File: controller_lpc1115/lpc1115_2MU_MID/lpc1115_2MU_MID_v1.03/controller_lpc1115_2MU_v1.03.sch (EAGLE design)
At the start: 57 parts, among them IC1 LPC1115, IC2 BD9G101, Q1 BC856, Q2 BC847C, Q3 BCP52, Q4 ASFL

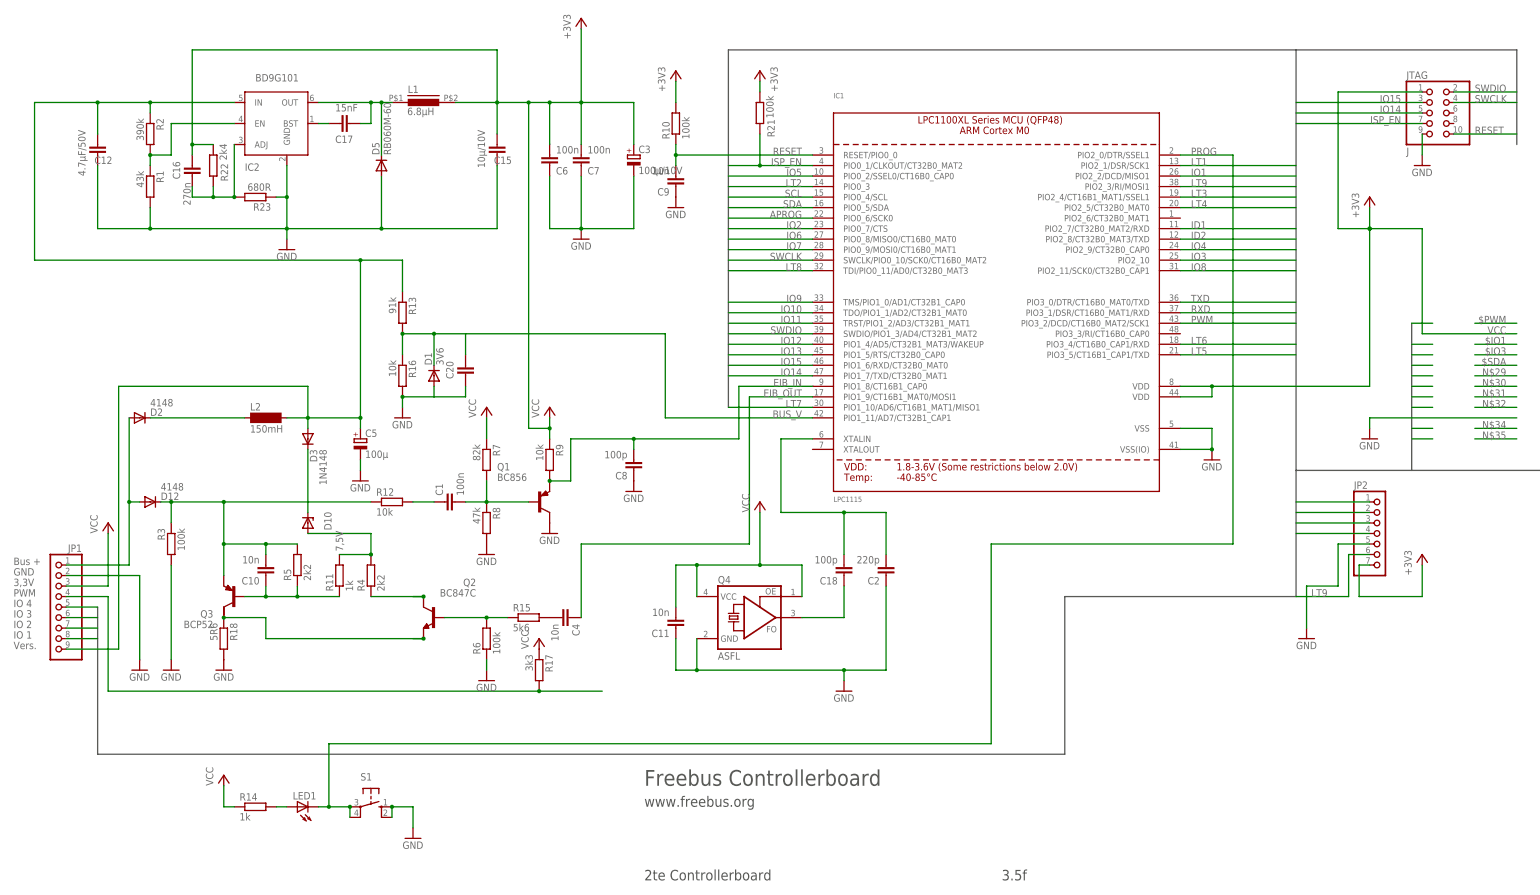
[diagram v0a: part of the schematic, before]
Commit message: Fix/add JP1 and JP2 pininfo for 2MU lpc1115 controller
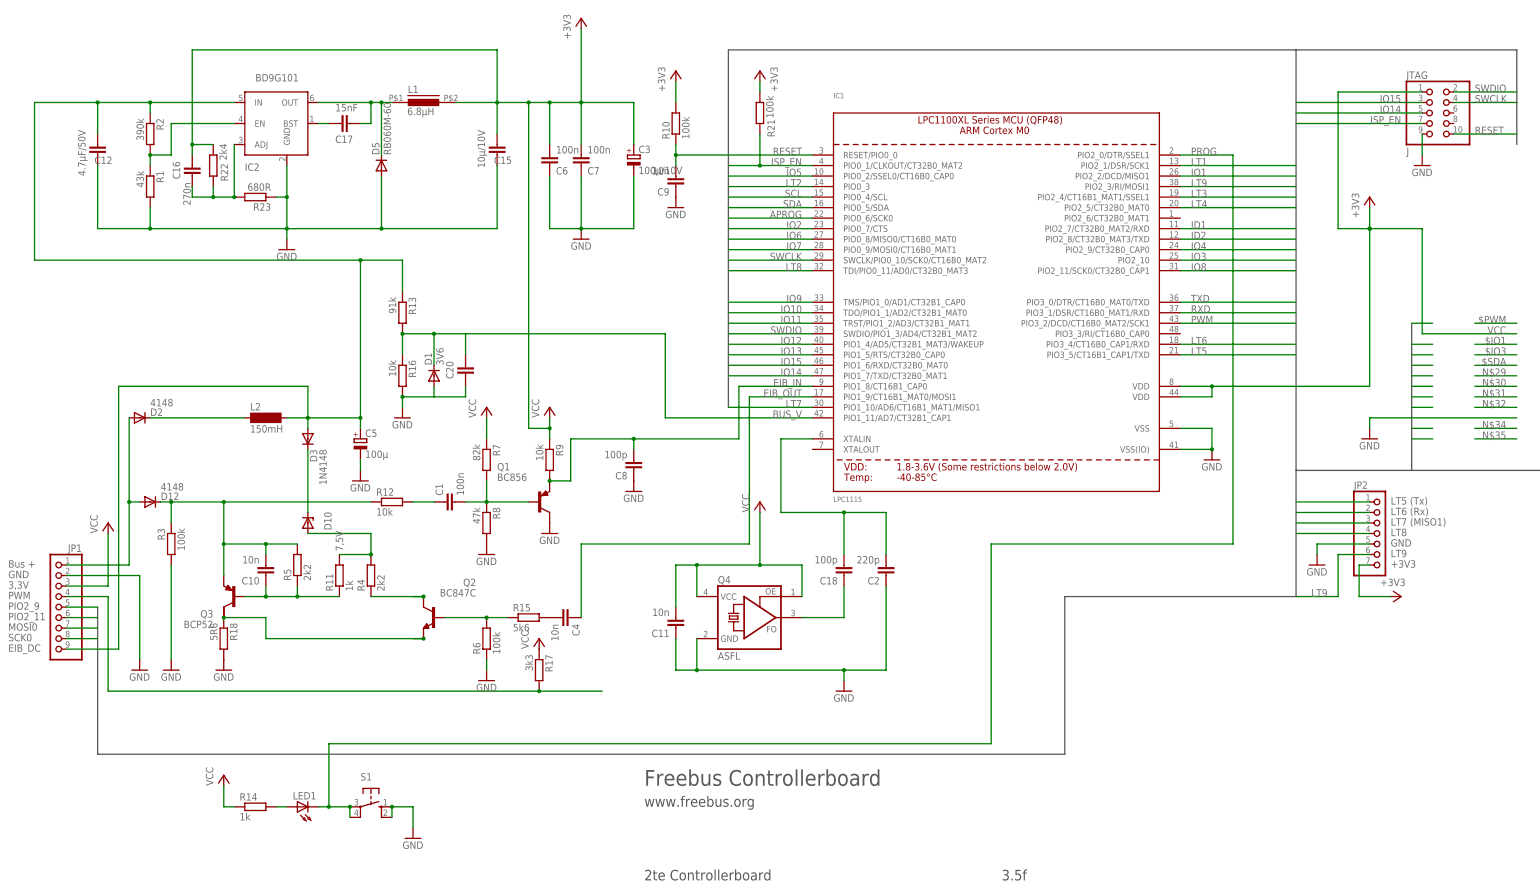
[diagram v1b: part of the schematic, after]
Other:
- note added: "+3V3"
- note added: "EIB_DC"
- note added: "LT5 (Tx)"
- note added: "LT6 (Rx)"
- note added: "LT7 (MISO1)"
- note added: "LT8"
- note added: "LT9"
- note added: "MOSI0"
- note added: "PIO2_11"
- note added: "PIO2_9"
- note added: "SCK0"
- note removed: "IO 1"
- note removed: "IO 2"
- note removed: "IO 3"
- note removed: "IO 4"
- note removed: "Vers."
